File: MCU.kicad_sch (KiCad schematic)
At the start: 42 parts, among them J1 SWD_LOG, SW1 SW_Push, U1 STM32F429IGTx, Y1 25MHz, Y5 32.768KHz

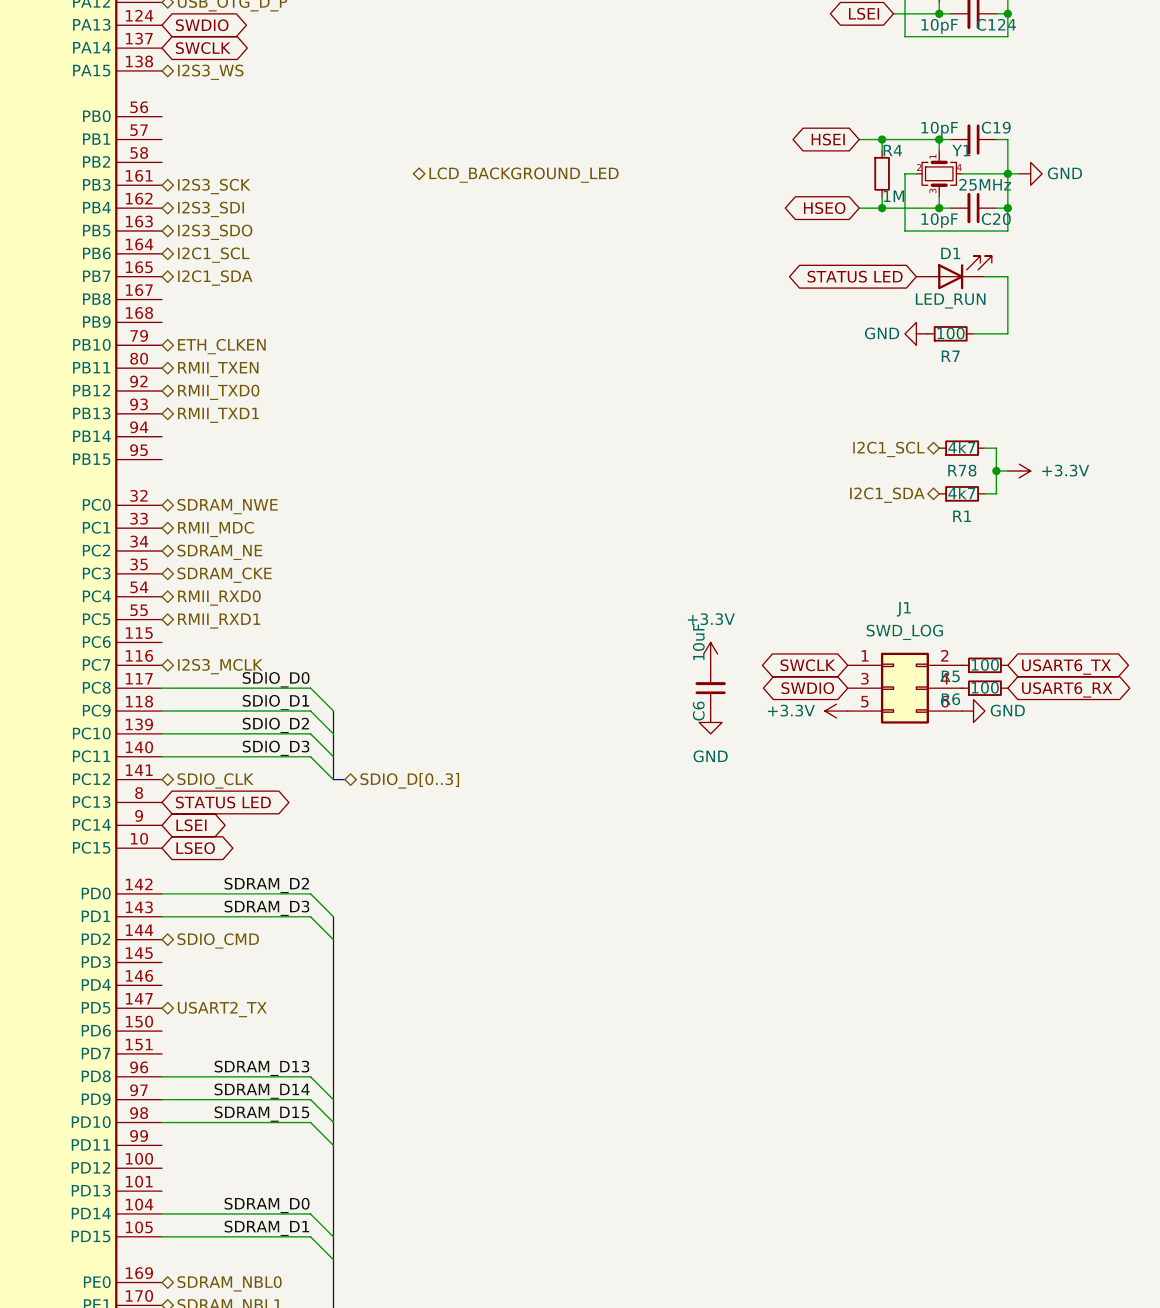
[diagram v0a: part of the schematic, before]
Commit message: Finish routing.
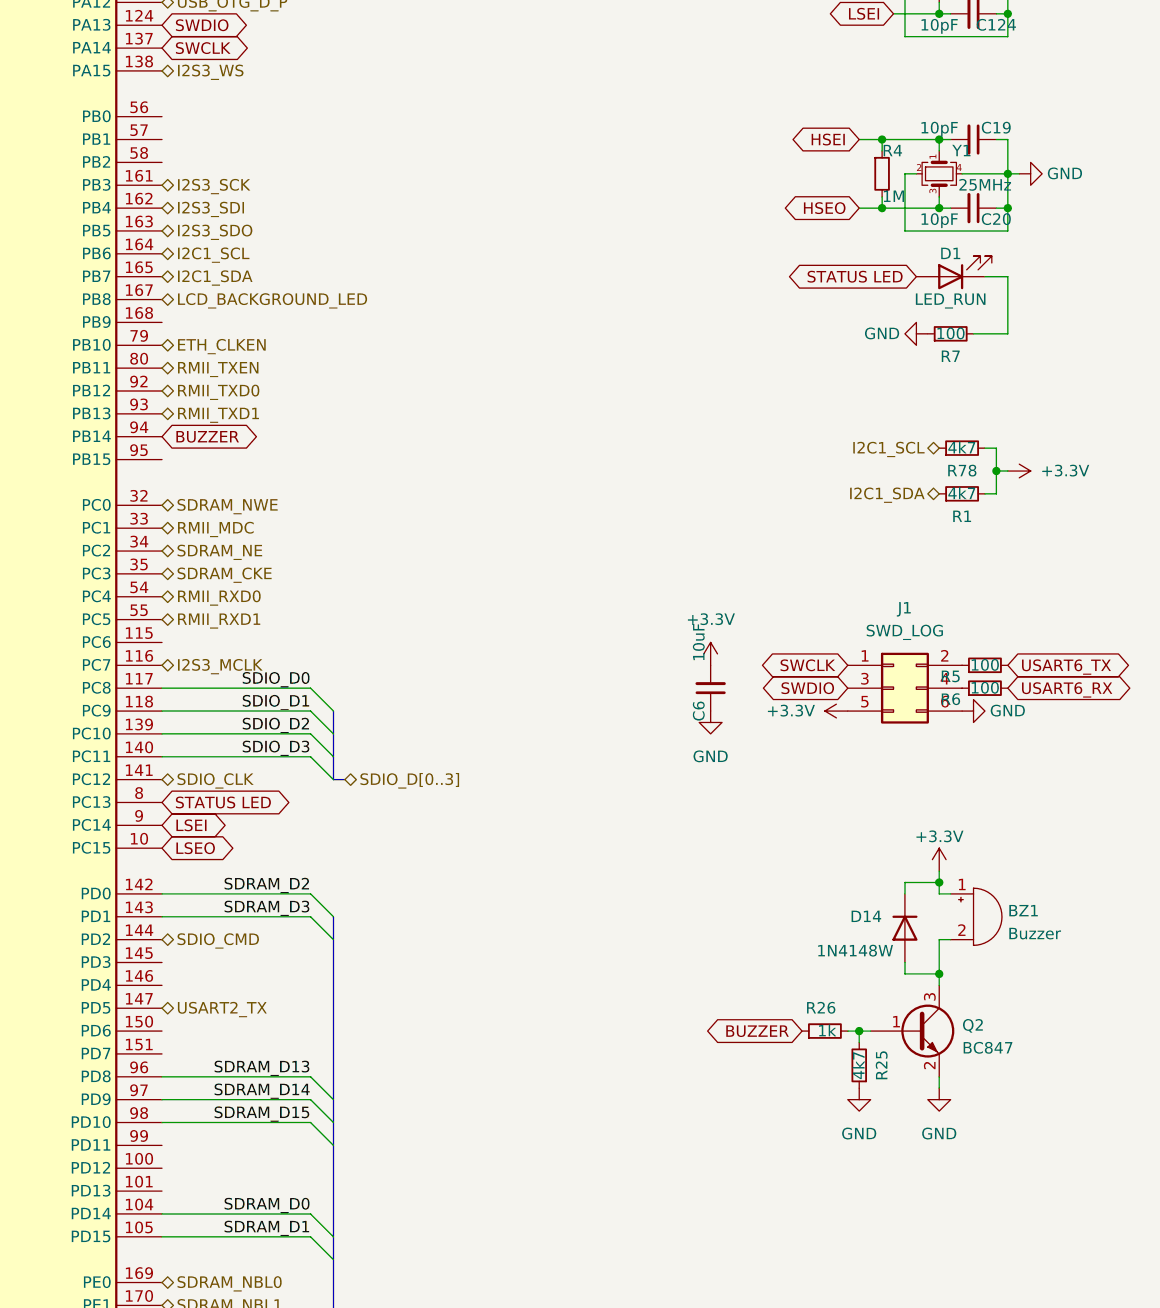
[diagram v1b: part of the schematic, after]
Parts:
- added BZ1: Buzzer, Buzzer_Beeper:MagneticBuzzer_ProSignal_ABT-410-RC, symbol Device:Buzzer
- added D14: 1N4148W, Diode_SMD:D_SOD-123F, symbol Diode:1N4148W
- added Q2: BC847, Anh_Footprints:SOT23-3, symbol Transistor_BJT:BC847
- added R25: 4k7, Anh_Footprints:R_0603, symbol Device:R_Small
- added R26: 1k, Anh_Footprints:R_0603, symbol Device:R_Small
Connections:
- net +3.3V: now also BZ1.1 (-), D14.1 (K)
- net GND: now also Q2.2 (E), R25.1
- net LCD_BACKGROUND_LED: now also U1.167 (PB8)
- net BUZZER: now reaches U1.94 (PB14)
- net BUZZER: now also R26.1
- new net: Q2.1 (B), R25.2, R26.2
- new net: BZ1.2 (+), D14.2 (A), Q2.3 (C)
